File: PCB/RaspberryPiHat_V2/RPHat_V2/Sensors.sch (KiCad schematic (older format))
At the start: 22 parts, among them IC1 TXB0108DQSR, J15 Conn_01x01, J2 Hall effect connector Right, J3 Halleffect Connector Left, U1 BME680, U2 INA219AxD, U3 ICM-20948, U4 GY-NEO6MV2

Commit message: Continued working on the pcb
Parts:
- C10, C11, C12, C14, C15, C6, C7: footprint Capacitor_SMD:C_0603_1608Metric_Pad1.08x0.95mm_HandSolder -> Capacitor_SMD:C_0402_1005Metric_Pad0.74x0.62mm_HandSolder
- IC1: symbol User:TXB0108DQSR -> RPHat_V2-rescue:TXB0108DQSR-User
- R7, R8: footprint Resistor_SMD:R_0603_1608Metric_Pad0.98x0.95mm_HandSolder -> Resistor_SMD:R_0402_1005Metric_Pad0.72x0.64mm_HandSolder
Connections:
- net labels added: IMU_INT_33
- wire segments 105 -> 107
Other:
- moved on the sheet: R8
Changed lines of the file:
@@
 	1    0    0    -1
 $EndComp
+Text GLabel 9600 2250 3    50   Input ~ 0
+GPS_RX
 Text GLabel 9400 2250 3    50   Input ~ 0
-GPS_RX
-Text GLabel 9600 2250 3    50   Input ~ 0
 GPS_TX
 $Comp
@@
 	9250 2100 9250 2250
 Wire Wire Line
+	9600 2100 9600 2250
+Wire Wire Line
 	9400 2100 9400 2250
-Wire Wire Line
-	9600 2100 9600 2250
 Wire Wire Line
 	9750 2100 9750 2250
@@
 Text GLabel 6350 1750 0    50   Input ~ 0
 SPI_CLK_18
-Text GLabel 6350 1850 0    50   Input ~ 0
+Text GLabel 5450 1850 0    50   Input ~ 0
 IMU_CS_18
 $Comp
@@
 Wire Wire Line
 	6850 1100 6850 1150
-Text GLabel 5550 2150 0    50   Input ~ 0
+Text GLabel 5450 2150 0    50   Input ~ 0
 IMU_INT_18
 $Comp
@@
 F 0 "R7" H 3670 1846 50  0000 L CNN
 F 1 "100k" H 3670 1755 50  0000 L CNN
-F 2 "Resistor_SMD:R_0603_1608Metric_Pad0.98x0.95mm_HandSolder" V 3530 1800 50  0001 C CNN
+F 2 "Resistor_SMD:R_0402_1005Metric_Pad0.72x0.64mm_HandSolder" V 3530 1800 50  0001 C CNN
 F 3 "~" H 3600 1800 50  0001 C CNN
 	1    3600 1800
@@
 L Device:R R8
 U 1 1 609401EF
-P 5700 1950
-F 0 "R8" H 5770 1996 50  0000 L CNN
-F 1 "100k" H 5770 1905 50  0000 L CNN
-F 2 "Resistor_SMD:R_0603_1608Metric_Pad0.98x0.95mm_HandSolder" V 5630 1950 50  0001 C CNN
-F 3 "~" H 5700 1950 50  0001 C CNN
-	1    5700 1950
+P 5550 1650
+F 0 "R8" H 5620 1696 50  0000 L CNN
+F 1 "100k" H 5620 1605 50  0000 L CNN
+F 2 "Resistor_SMD:R_0402_1005Metric_Pad0.72x0.64mm_HandSolder" V 5480 1650 50  0001 C CNN
+F 3 "~" H 5550 1650 50  0001 C CNN
+	1    5550 1650
 	1    0    0    -1
 $EndComp
@@
 L power:+1V8 #PWR0125
 U 1 1 609401F5
-P 5700 1750
-F 0 "#PWR0125" H 5700 1600 50  0001 C CNN
-F 1 "+1V8" H 5715 1923 50  0000 C CNN
-F 2 "" H 5700 1750 50  0001 C CNN
-F 3 "" H 5700 1750 50  0001 C CNN
-	1    5700 1750
-	1    0    0    -1
-$EndComp
-Wire Wire Line
-	5700 1750 5700 1800
+P 5550 1450
+F 0 "#PWR0125" H 5550 1300 50  0001 C CNN
+F 1 "+1V8" H 5565 1623 50  0000 C CNN
+F 2 "" H 5550 1450 50  0001 C CNN
+F 3 "" H 5550 1450 50  0001 C CNN
+	1    5550 1450
+	1    0    0    -1
+$EndComp
+Wire Wire Line
+	5550 1450 5550 1500
 $Comp
 L Device:C C7
@@
 F 0 "C7" H 1615 1496 50  0000 L CNN
 F 1 "100nF" H 1615 1405 50  0000 L CNN
-F 2 "Capacitor_SMD:C_0603_1608Metric_Pad1.08x0.95mm_HandSolder" H 1538 1300 50  0001 C CNN
+F 2 "Capacitor_SMD:C_0402_1005Metric_Pad0.74x0.62mm_HandSolder" H 1538 1300 50  0001 C CNN
 F 3 "~" H 1500 1450 50  0001 C CNN
 	1    1500 1450
@@
 F 0 "C6" H 1165 1496 50  0000 L CNN
 F 1 "100nF" H 1165 1405 50  0000 L CNN
-F 2 "Capacitor_SMD:C_0603_1608Metric_Pad1.08x0.95mm_HandSolder" H 1088 1300 50  0001 C CNN
+F 2 "Capacitor_SMD:C_0402_1005Metric_Pad0.74x0.62mm_HandSolder" H 1088 1300 50  0001 C CNN
 F 3 "~" H 1050 1450 50  0001 C CNN
 	1    1050 1450
@@
 F 0 "C11" H 7815 2246 50  0000 L CNN
 F 1 "100nF" H 7815 2155 50  0000 L CNN
-F 2 "Capacitor_SMD:C_0603_1608Metric_Pad1.08x0.95mm_HandSolder" H 7738 2050 50  0001 C CNN
+F 2 "Capacitor_SMD:C_0402_1005Metric_Pad0.74x0.62mm_HandSolder" H 7738 2050 50  0001 C CNN
 F 3 "~" H 7700 2200 50  0001 C CNN
 	1    7700 2200
@@
 F 0 "C10" H 7765 1446 50  0000 L CNN
 F 1 "100nF" H 7765 1355 50  0000 L CNN
-F 2 "Capacitor_SMD:C_0603_1608Metric_Pad1.08x0.95mm_HandSolder" H 7688 1250 50  0001 C CNN
+F 2 "Capacitor_SMD:C_0402_1005Metric_Pad0.74x0.62mm_HandSolder" H 7688 1250 50  0001 C CNN
 F 3 "~" H 7650 1400 50  0001 C CNN
 	1    7650 1400
@@
 F 0 "C12" H 8215 1446 50  0000 L CNN
 F 1 "100nF" H 8215 1355 50  0000 L CNN
-F 2 "Capacitor_SMD:C_0603_1608Metric_Pad1.08x0.95mm_HandSolder" H 8138 1250 50  0001 C CNN
+F 2 "Capacitor_SMD:C_0402_1005Metric_Pad0.74x0.62mm_HandSolder" H 8138 1250 50  0001 C CNN
 F 3 "~" H 8100 1400 50  0001 C CNN
 	1    8100 1400
@@
 HE_R_OUTPUT
 $Comp
-L power:+1V8 #PWR0130
-U 1 1 609C23EB
+L power:+3V3 #PWR0131
+U 1 1 609C3DE0
 P 5650 5300
-F 0 "#PWR0130" H 5650 5150 50  0001 C CNN
-F 1 "+1V8" H 5665 5473 50  0000 C CNN
+F 0 "#PWR0131" H 5650 5150 50  0001 C CNN
+F 1 "+3V3" H 5665 5473 50  0000 C CNN
 F 2 "" H 5650 5300 50  0001 C CNN
 F 3 "" H 5650 5300 50  0001 C CNN
 	1    5650 5300
-	1    0    0    -1
-$EndComp
-$Comp
-L power:+3V3 #PWR0131
-U 1 1 609C3DE0
-P 8550 5400
-F 0 "#PWR0131" H 8550 5250 50  0001 C CNN
-F 1 "+3V3" H 8565 5573 50  0000 C CNN
-F 2 "" H 8550 5400 50  0001 C CNN
-F 3 "" H 8550 5400 50  0001 C CNN
-	1    8550 5400
 	1    0    0    -1
 $EndComp
@@
 	6350 1750 6450 1750
 Wire Wire Line
-	6350 1850 6450 1850
-Wire Wire Line
-	5550 2150 5700 2150
-Wire Wire Line
-	5700 2100 5700 2150
-Connection ~ 5700 2150
-Wire Wire Line
-	5700 2150 6450 2150
-Wire Wire Line
 	2950 1400 2900 1400
 Wire Wire Line
@@
 Wire Wire Line
 	3600 1600 3600 1650
-$Comp
-L power:GNDREF #PWR0138
-U 1 1 60B79349
-P 1300 1650
-F 0 "#PWR0138" H 1300 1400 50  0001 C CNN
-F 1 "GNDREF" H 1305 1477 50  0001 C CNN
-F 2 "" H 1300 1650 50  0001 C CNN
-F 3 "" H 1300 1650 50  0001 C CNN
-	1    1300 1650
-	1    0    0    -1
-$EndComp
-Wire Wire Line
-	1500 1600 1500 1650
-Wire Wire Line
-	1500 1650 1300 1650
-Wire Wire Line
-	1050 1600 1050 1650
-Wire Wire Line
-	1050 1650 1300 1650
-Connection ~ 1300 1650
 $Comp
 L Device:C C14
@@
 F 0 "C14" H 8665 5696 50  0000 L CNN
 F 1 "100nF" H 8665 5605 50  0000 L CNN
-F 2 "Capacitor_SMD:C_0603_1608Metric_Pad1.08x0.95mm_HandSolder" H 8588 5500 50  0001 C CNN
+F 2 "Capacitor_SMD:C_0402_1005Metric_Pad0.74x0.62mm_HandSolder" H 8588 5500 50  0001 C CNN
 F 3 "~" H 8550 5650 50  0001 C CNN
 	1    8550 5650
@@
 F 0 "C15" H 5765 5596 50  0000 L CNN
 F 1 "100nF" H 5765 5505 50  0000 L CNN
-F 2 "Capacitor_SMD:C_0603_1608Metric_Pad1.08x0.95mm_HandSolder" H 5688 5400 50  0001 C CNN
+F 2 "Capacitor_SMD:C_0402_1005Metric_Pad0.74x0.62mm_HandSolder" H 5688 5400 50  0001 C CNN
 F 3 "~" H 5650 5550 50  0001 C CNN
 	1    5650 5550
@@
 	2700 6600 2700 6850
 $Comp
-L User:TXB0108DQSR IC1
+L RPHat_V2-rescue:TXB0108DQSR-User IC1
 U 1 1 60AA4FBA
 P 6600 5000
+AR Path="/60AA4FBA" Ref="IC1"  Part="1"
+AR Path="/6092276E/60AA4FBA" Ref="IC1"  Part="1"
 F 0 "IC1" H 7150 5265 50  0000 C CNN
 F 1 "TXB0108DQSR" H 7150 5174 50  0000 C CNN
@@
 Connection ~ 6500 5400
 Connection ~ 5650 5400
+Wire Wire Line
+	1500 2400 2200 2400
+Wire Wire Line
+	1500 1600 1500 2400
+Connection ~ 2200 2400
+Wire Wire Line
+	1050 2400 1500 2400
+Wire Wire Line
+	1050 1600 1050 2400
+Connection ~ 1500 2400
+Wire Wire Line
+	5550 1800 5550 1850
+Connection ~ 5550 1850
+Wire Wire Line
+	5550 1850 5450 1850
+Wire Wire Line
+	5550 1850 6450 1850
+Wire Wire Line
+	5450 2150 6450 2150
+Text GLabel 7750 5200 2    50   Input ~ 0
+IMU_INT_18
+Wire Wire Line
+	7750 5200 7700 5200
+Text GLabel 6550 5700 0    50   Input ~ 0
+IMU_INT_33
+Wire Wire Line
+	6550 5700 6600 5700
+$Comp
+L power:+1V8 #PWR0130
+U 1 1 60C17D10
+P 8550 5400
+F 0 "#PWR0130" H 8550 5250 50  0001 C CNN
+F 1 "+1V8" H 8565 5573 50  0000 C CNN
+F 2 "" H 8550 5400 50  0001 C CNN
+F 3 "" H 8550 5400 50  0001 C CNN
+	1    8550 5400
+	1    0    0    -1
+$EndComp
 $EndSCHEMATC

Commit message: Never gonna give you up
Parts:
- U4: footprint Connector_PinHeader_2.54mm:PinHeader_1x04_P2.54mm_Vertical -> User:GY-NEO6MV2
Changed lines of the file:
@@
 F 0 "U4" H 9878 1838 50  0000 L CNN
 F 1 "GY-NEO6MV2" H 9878 1747 50  0000 L CNN
-F 2 "Connector_PinHeader_2.54mm:PinHeader_1x04_P2.54mm_Vertical" H 9500 2150 50  0001 C CNN
+F 2 "User:GY-NEO6MV2" H 9500 2150 50  0001 C CNN
 F 3 "" H 9500 2250 50  0001 C CNN
 	1    9500 1800

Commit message: working on pcb Ja!
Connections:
- net SPI_MISO_18: now also IC1.20 (B1); no longer IC1.19 (B2)
- net SPI_MISO_33: now also IC1.1 (A1); no longer IC1.2 (A2)
- net SPI_MOSI_18: now also IC1.19 (B2); no longer IC1.20 (B1)
- net SPI_MOSI_33: now also IC1.2 (A2); no longer IC1.1 (A1)
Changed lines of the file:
@@
 Text GLabel 7750 5300 2    50   Input ~ 0
 BME_CS_18
+Text GLabel 6500 5000 0    50   Input ~ 0
+SPI_MISO_33
 Text GLabel 6500 5100 0    50   Input ~ 0
-SPI_MISO_33
-Text GLabel 6500 5000 0    50   Input ~ 0
 SPI_MOSI_33
 Text GLabel 6500 5200 0    50   Input ~ 0
@@
 	7750 5300 7700 5300
 Wire Wire Line
+	7800 5900 7700 5900
+Wire Wire Line
 	7800 5800 7700 5800
 Wire Wire Line
-	7800 5900 7700 5900
-Wire Wire Line
 	7800 5700 7700 5700
 Wire Wire Line
 	7800 5600 7700 5600
 Wire Wire Line
+	6500 5100 6600 5100
+Wire Wire Line
 	6500 5000 6600 5000
-Wire Wire Line
-	6500 5100 6600 5100
 Wire Wire Line
 	6500 5300 6600 5300
@@
 	8550 5500 8550 5400
 Connection ~ 8550 5500
+Text GLabel 7800 5800 2    50   Input ~ 0
+SPI_MOSI_18
 Text GLabel 7800 5900 2    50   Input ~ 0
-SPI_MOSI_18
-Text GLabel 7800 5800 2    50   Input ~ 0
 SPI_MISO_18
 Wire Wire Line

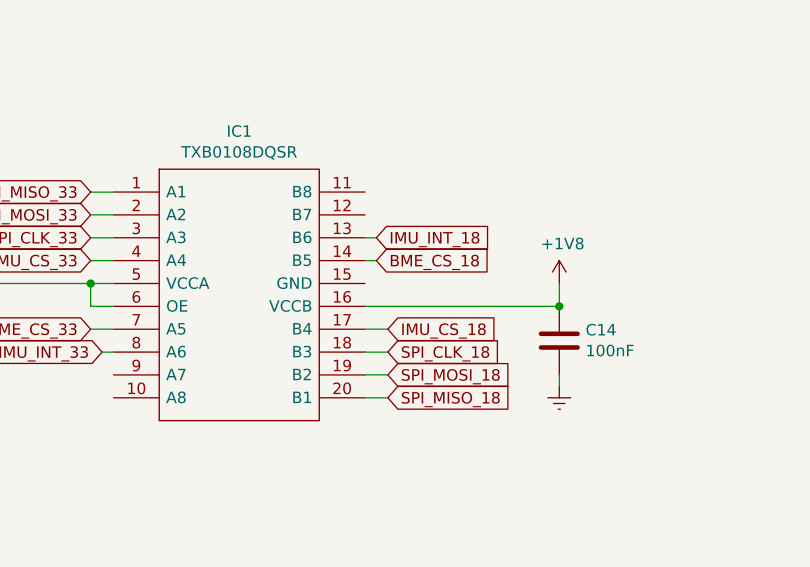
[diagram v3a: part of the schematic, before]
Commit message: Fixed linking issue and finished pcb
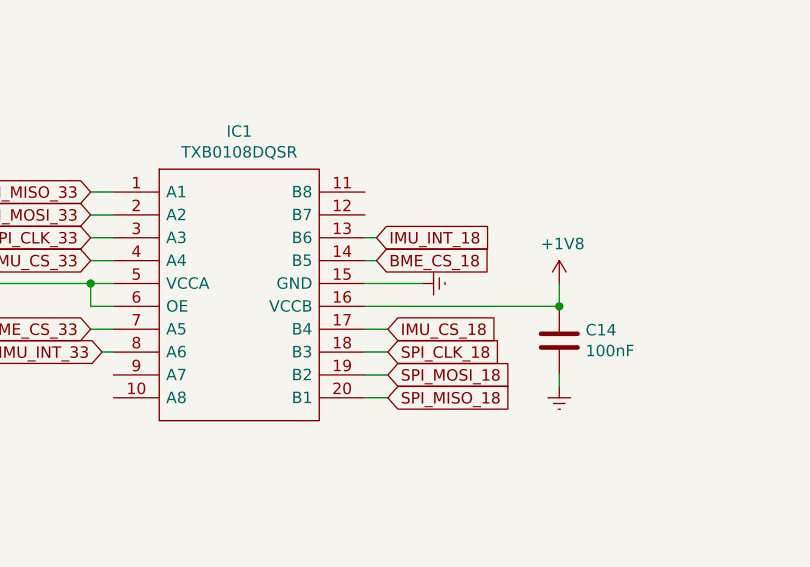
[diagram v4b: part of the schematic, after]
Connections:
- net GNDREF: now also IC1.15 (GND)
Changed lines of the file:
@@
 	1    0    0    -1
 $EndComp
+$Comp
+L power:GNDREF #PWR?
+U 1 1 60EA1BC4
+P 7950 5400
+F 0 "#PWR?" H 7950 5150 50  0001 C CNN
+F 1 "GNDREF" H 7955 5227 50  0001 C CNN
+F 2 "" H 7950 5400 50  0001 C CNN
+F 3 "" H 7950 5400 50  0001 C CNN
+	1    7950 5400
+	0    -1   -1   0
+$EndComp
+Wire Wire Line
+	7700 5400 7950 5400
 $EndSCHEMATC
